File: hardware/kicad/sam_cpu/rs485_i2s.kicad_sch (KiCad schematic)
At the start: 15 parts, among them J27 J27 RS485, J28 J28 I2S IN, U32 THVD1450

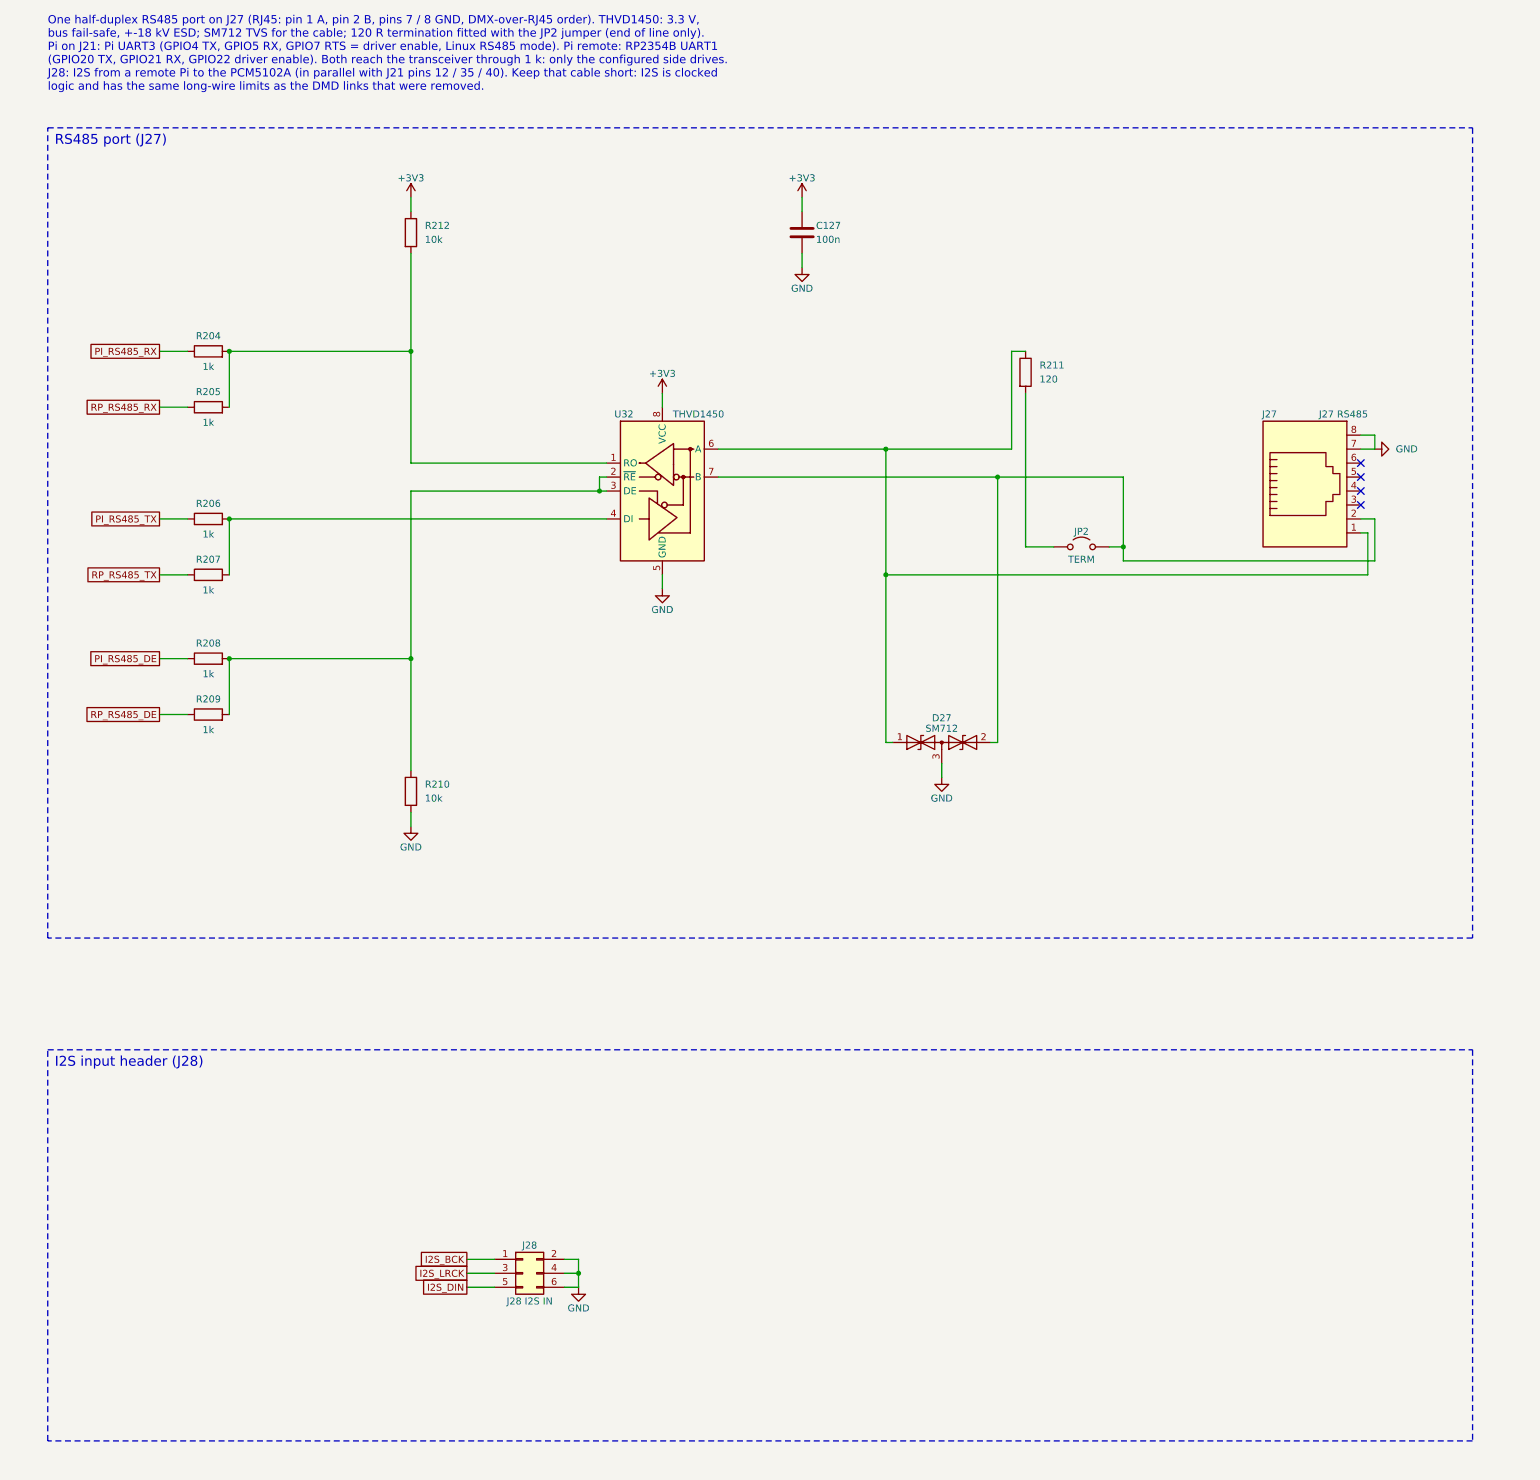
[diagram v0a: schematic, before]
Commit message: Isolated RS485 (ADM2682E, two top-entry RJ45s), line-in jack, board extension back, MH3 lowered
- Page 13: ADM2682E with the cable side on GND_ISO, J27 in / J29 out (OST PJ012
  vertical), J30 switched 3.5 mm line-in between the DAC and the amplifiers.
- Audio sheet: DAC output wires split into AUD_DAC_L/R and AUD_AMP_L/R for J30.
- Board: 142 mm extension below the Pi restored, GND_ISO zone with a 2 mm gap,
  MH3 screw position moved down 7.42 mm (open notch), page-13 parts re-placed.
- Change scripts c16-c18; ERC 0, DRC schematic parity 0.

Co-Authored-By: Claude Opus 5.5 (1M context) <noreply@anthropic.com>
Claude-Session: https://claude.ai/code/session_01ExuDVoDDDHhVWjb8EwVzYb
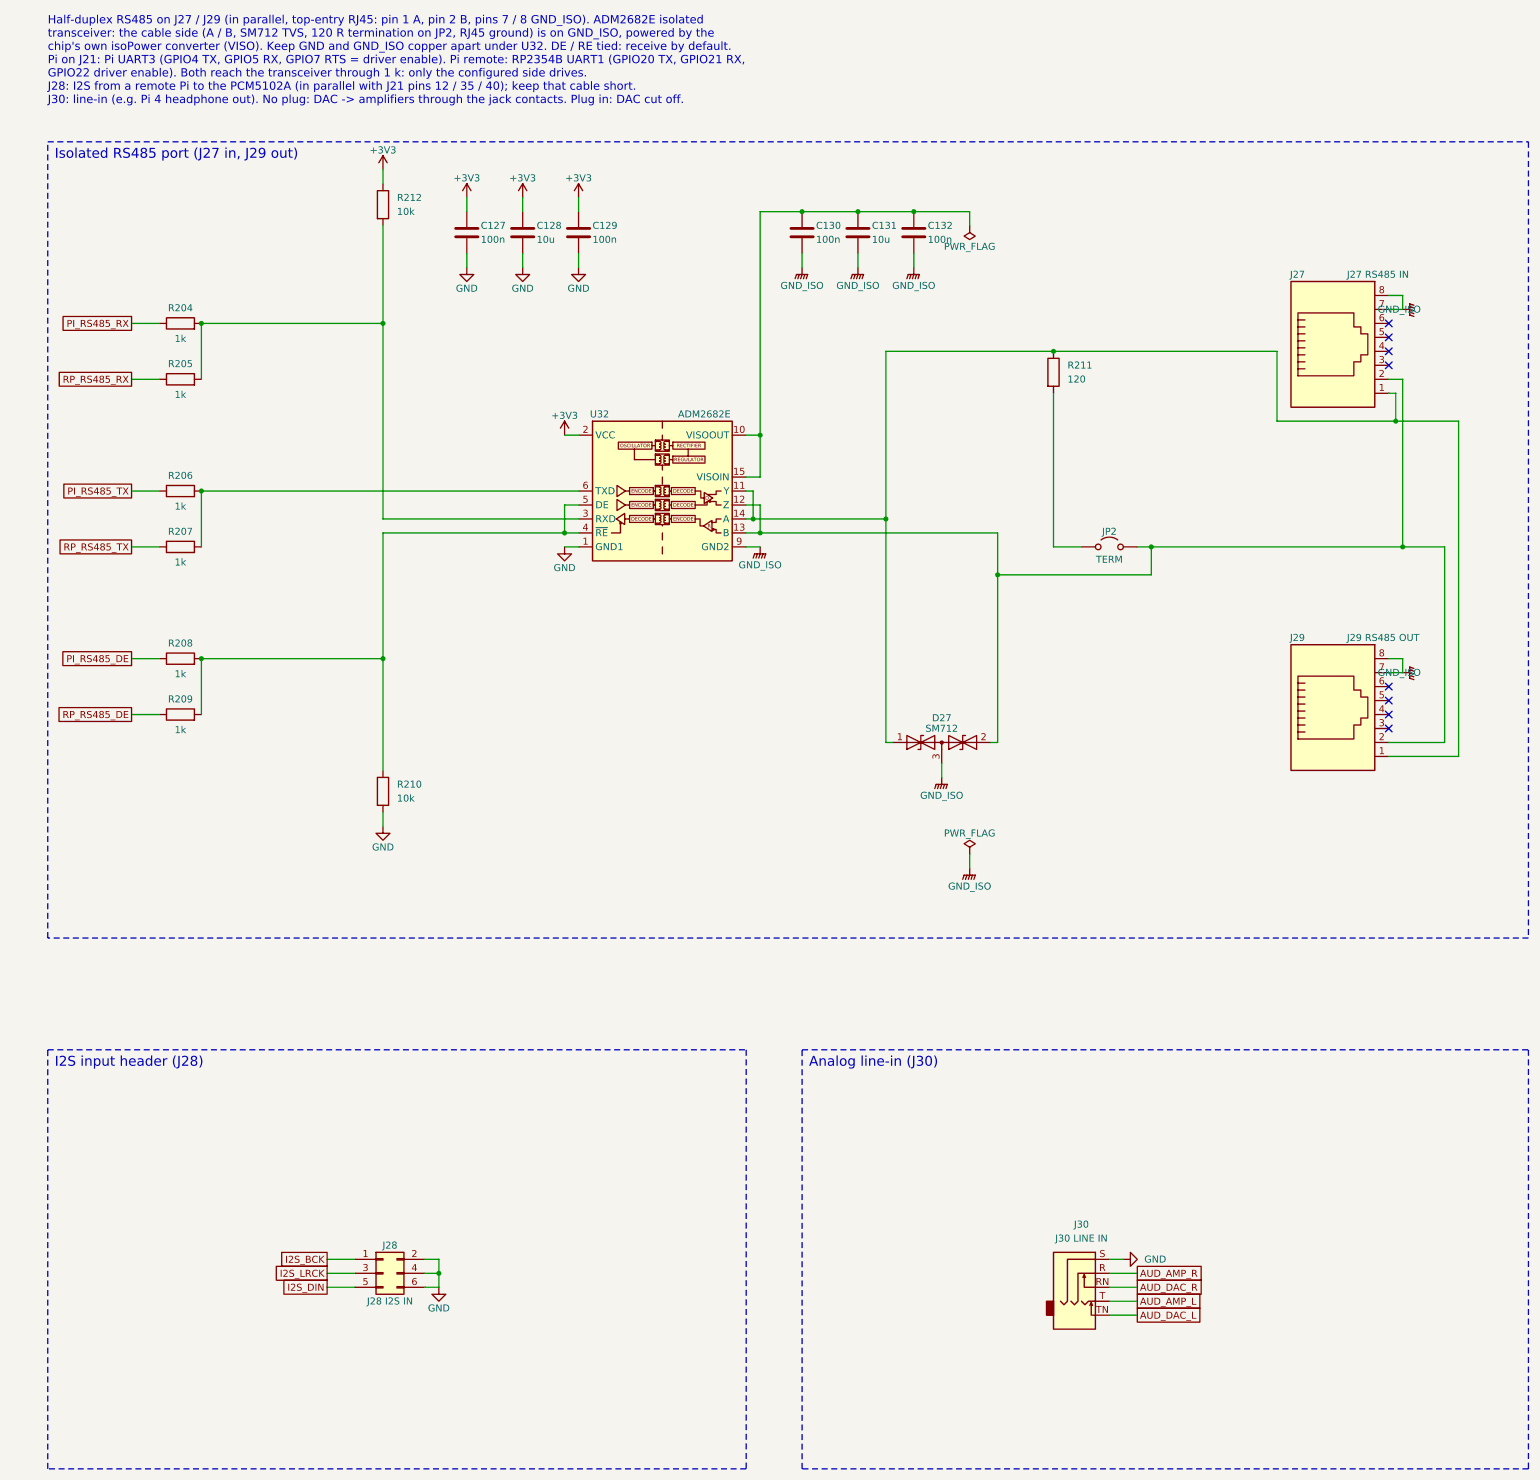
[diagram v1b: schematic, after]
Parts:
- added C128, C131: 10u, Capacitor_SMD:C_0805_2012Metric, symbol Device:C
- added C129, C130, C132: 100n, Capacitor_SMD:C_0603_1608Metric, symbol Device:C
- added J29: J29 RS485 OUT, Connector_RJ:RJ45_OST_PJ012-8P8CX_Vertical, symbol Connector:RJ45
- added J30: J30 LINE IN, Connector_Audio:Jack_3.5mm_CUI_SJ1-3535NG_Horizontal, symbol Connector_Audio:AudioJack3_SwitchTR
- J27: value J27 RS485 -> J27 RS485 IN; footprint Connector_RJ:RJ45_Amphenol_54602-x08_Horizontal -> Connector_RJ:RJ45_OST_PJ012-8P8CX_Vertical
- U32: value THVD1450 -> ADM2682E; footprint Package_SO:SOIC-8_3.9x4.9mm_P1.27mm -> Package_SO:SOIC-16W_7.5x12.8mm_P1.27mm; symbol Interface_UART:THVD1450D -> Interface_UART:ADM2682E
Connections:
- net +3V3: now also U32.2 (VCC), U32.7 (VCC), C128.1, C129.1; no longer U32.8 (VCC)
- net GND: now also U32.1 (GND1), U32.8 (GND1), C128.2, C129.2, J30.S; no longer D27.3 (common), J27.7, J27.8, U32.5 (GND)
- net at R204.2, R205.2, R212.2: now also U32.3 (RXD); no longer U32.1 (RO)
- net at R208.2, R209.2, R210.1: now also U32.4 (~{RE}), U32.5 (DE); no longer U32.2 (~{RE}), U32.3 (DE)
- net at R206.2, R207.2: now also U32.6 (TXD); no longer U32.4 (DI)
- net at D27.1 (A1), J27.1, R211.1: now also U32.11 (Y), U32.14 (A), J29.1; no longer U32.6 (A)
- net at D27.2 (A2), J27.2, JP2.2 (B): now also U32.12 (Z), U32.13 (B), J29.2; no longer U32.7 (B)
- new net: C130.1, C131.1, C132.1, U32.10 (VISOOUT), U32.15 (VISOIN)
- new net AUD_AMP_L: J30.T
- new net AUD_AMP_R: J30.R
- new net AUD_DAC_L: J30.TN
- new net AUD_DAC_R: J30.RN
- new net GND_ISO: C130.2, C131.2, C132.2, D27.3 (common), J27.7, J27.8, J29.7, J29.8, U32.16 (GND2), U32.9 (GND2)
- no-connect marks 4 -> 8
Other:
- note added: "Analog line-in (J30)"
- note added: "Half-duplex RS485 on J27 / J29 (in parallel, top-entry RJ45: pin 1 A, pin 2 B, pins 7 / 8 GND_ISO). ADM2682E isolated transceiver: the cable side (A / B, SM712 TVS, 120 R termination on JP2, RJ45 ground) is on GND_ISO, powered by the chip's own isoPower converter (VISO). Keep GND and GND_ISO copper apart under U32. DE / RE tied: receive by default. Pi on J21: Pi UART3 (GPIO4 TX, GPIO5 RX, GPIO7 R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"
- note added: "Isolated RS485 port (J27 in, J29 out)"
- note removed: "One half-duplex RS485 port on J27 (RJ45: pin 1 A, pin 2 B, pins 7 / 8 GND, DMX-over-RJ45 order). THVD1450: 3.3 V, bus fail-safe, +-18 kV ESD; SM712 TVS for the cable; 120 R termination fitted with the JP2 jumper (end of line only). Pi on J21: Pi UART3 (GPIO4 TX, GPIO5 RX, GPIO7 RTS = driver enable, Linux RS485 mode). Pi remote: RP2354B UART1 (GPIO20 TX, GPIO21 RX, GPIO22 driver enable). Both reac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"
- note removed: "RS485 port (J27)"
- title: RS485 port (RJ45) and I2S input header -> Isolated RS485 port (2x RJ45), I2S input header, analog line-in
- moved on the sheet: C127, J27, J28, JP2, R204, R205, R206, R207, R208, R209, R210, R211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

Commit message: U32 CA-IS2092VW, BT1 XDCR-2032, J27/J29 side-entry RJ45 for JLCPCB stock
Replace parts JLCPCB does not stock: U32 ADM2682E -> CA-IS2092VW (new symbol,
pinout remap), BT1 Keystone 3034 -> Lianxin XDCR-2032-603, J27/J29 OST PJ012 ->
CONNFLY DS1128-05-S8B8P side-entry at the right edge. Isolated side and BT1
rerouted; project footprint library sam_cpu.pretty added.

Co-Authored-By: Claude Opus 5.5 (1M context) <noreply@anthropic.com>
Claude-Session: https://claude.ai/code/session_01ExuDVoDDDHhVWjb8EwVzYb
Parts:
- J27, J29: footprint Connector_RJ:RJ45_OST_PJ012-8P8CX_Vertical -> sam_cpu:RJ45_Connfly_DS1128-05-S8B8P_Horizontal
- U32: value ADM2682E -> CA-IS2092VW; symbol Interface_UART:ADM2682E -> sam_cpu:CA-IS2092VW
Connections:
- net +3V3: now also U32.1 (VCC); no longer U32.2 (VCC)
- net GND: now also U32.2 (GNDA); no longer U32.1 (GND1)
- net GND_ISO: now also U32.15 (GNDB); no longer U32.16 (GND2)
- net at C130.1, C131.1, C132.1: now also U32.14 (VISOIN), U32.16 (VISO); no longer U32.10 (VISOOUT), U32.15 (VISOIN)
- net at D27.1 (A1), J27.1, J29.1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: now also U32.12 (A); no longer U32.11 (Y), U32.14 (A)
- net at D27.2 (A2), J27.2, J29.2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: no longer U32.12 (Z)
- no-connect marks 8 -> 10
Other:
- note added: "Half-duplex RS485 on J27 / J29 (in parallel, top-entry RJ45: pin 1 A, pin 2 B, pins 7 / 8 GND_ISO). CA-IS2092VW isolated transceiver: the cable side (A / B, SM712 TVS, 120 R termination on JP2, RJ45 ground) is on GND_ISO, powered by the chip's own isolated DC-DC (VISO 3.3 V, SEL open). Keep GND and GND_ISO copper apart under U32. DE / RE tied: receive by default. Pi on J21: Pi UART3 (GPIO4 TX, GP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"
- note removed: "Half-duplex RS485 on J27 / J29 (in parallel, top-entry RJ45: pin 1 A, pin 2 B, pins 7 / 8 GND_ISO). ADM2682E isolated transceiver: the cable side (A / B, SM712 TVS, 120 R termination on JP2, RJ45 ground) is on GND_ISO, powered by the chip's own isoPower converter (VISO). Keep GND and GND_ISO copper apart under U32. DE / RE tied: receive by default. Pi on J21: Pi UART3 (GPIO4 TX, GPIO5 RX, GPIO7 R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"
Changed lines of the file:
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@@
 		)
 	)
-	(text "Half-duplex RS485 on J27 / J29 (in parallel, top-entry RJ45: pin 1 A, pin 2 B, pins 7 / 8 GND_ISO). ADM2682E isolated\ntransceiver: the cable side (A / B, SM712 TVS, 120 R termination on JP2, RJ45 ground) is on GND_ISO, powered by the\nchip's own isoPower converter (VISO). Keep GND and GND_ISO copper apart under U32. DE / RE tied: receive by default.\nPi on J21: Pi UART3 (GPIO4 TX, GPIO5 RX, GPIO7 RTS = driver enable). Pi remote: RP2354B UART1 (GPIO20 TX, GPIO21 RX,\nGPIO22 driver enable). Both reach the transceiver through 1 k: only the configured side drives.\nJ28: I2S from a remote Pi to the PCM5102A (in parallel with J21 pins 12 / 35 / 40); keep that cable short.\nJ30: line-in (e.g. Pi 4 headphone out). No plug: DAC -> amplifiers through the jack contacts. Plug in: DAC cut off."
+	(text "Half-duplex RS485 on J27 / J29 (in parallel, top-entry RJ45: pin 1 A, pin 2 B, pins 7 / 8 GND_ISO). CA-IS2092VW isolated\ntransceiver: the cable side (A / B, SM712 TVS, 120 R termination on JP2, RJ45 ground) is on GND_ISO, powered by the\nchip's own isolated DC-DC (VISO 3.3 V, SEL open). Keep GND and GND_ISO copper apart under U32. DE / RE tied: receive by default.\nPi on J21: Pi UART3 (GPIO4 TX, GPIO5 RX, GPIO7 RTS = driver enable). Pi remote: RP2354B UART1 (GPIO20 TX, GPIO21 RX,\nGPIO22 driver enable). Both reach the transceiver through 1 k: only the configured side drives.\nJ28: I2S from a remote Pi to the PCM5102A (in parallel with J21 pins 12 / 35 / 40); keep that cable short.\nJ30: line-in (e.g. Pi 4 headphone out). No plug: DAC -> amplifiers through the jack contacts. Plug in: DAC cut off."
 		(exclude_from_sim no)
 		(at 15.24 15.24 0)
@@
 	)
 	(junction
-		(at 143.51 106.68)
-		(diameter 0)
-		(color 0 0 0 0)
-	)
-	(junction
 		(at 43.18 101.6)
 		(diameter 0)
@@
 	)
 	(junction
-		(at 144.78 109.22)
-		(diameter 0)
-		(color 0 0 0 0)
-	)
-	(junction
 		(at 43.18 132.08)
 		(diameter 0)
@@
 		(at 259.08 142.24)
 	)
+	(no_connect
+		(at 142.24 101.6)
+	)
+	(no_connect
+		(at 142.24 104.14)
+	)
 	(wire
 		(pts
@@
 	(wire
 		(pts
-			(xy 142.24 101.6) (xy 143.51 101.6)
-		)
-		(stroke
-			(width 0)
-			(type default)
-		)
-	)
-	(wire
-		(pts
 			(xy 144.78 99.06) (xy 142.24 99.06)
 		)
@@
 	(wire
 		(pts
-			(xy 144.78 104.14) (xy 144.78 109.22)
-		)
-		(stroke
-			(width 0)
-			(type default)
-		)
-	)
-	(wire
-		(pts
 			(xy 142.24 111.76) (xy 144.78 111.76)
 		)
@@
 	(wire
 		(pts
-			(xy 143.51 101.6) (xy 143.51 106.68)
-		)
-		(stroke
-			(width 0)
-			(type default)
-		)
-	)
-	(wire
-		(pts
 			(xy 208.28 248.92) (xy 213.36 248.92)
 		)
@@
 	(wire
 		(pts
-			(xy 142.24 104.14) (xy 144.78 104.14)
-		)
-		(stroke
-			(width 0)
-			(type default)
-		)
-	)
-	(wire
-		(pts
 			(xy 167.64 106.68) (xy 167.64 76.2)
 		)
@@
 	)
 	(symbol
-		(lib_id "Interface_UART:ADM2682E")
+		(lib_id "sam_cpu:CA-IS2092VW")
 		(at 127 101.6 0)
 		(unit 1)
@@
 			)
 		)
-		(property "Value" "ADM2682E"
+		(property "Value" "CA-IS2092VW"
 			(at 134.62 87.63 0)
 			(show_name no)
@@
 			)
 		)
-		(property "Footprint" "Connector_RJ:RJ45_OST_PJ012-8P8CX_Vertical"
+		(property "Footprint" "sam_cpu:RJ45_Connfly_DS1128-05-S8B8P_Horizontal"
 			(at 248.92 141.605 90)
 			(hide yes)
@@
 			)
 		)
-		(property "Footprint" "Connector_RJ:RJ45_OST_PJ012-8P8CX_Vertical"
+		(property "Footprint" "sam_cpu:RJ45_Connfly_DS1128-05-S8B8P_Horizontal"
 			(at 248.92 75.565 90)
 			(hide yes)
